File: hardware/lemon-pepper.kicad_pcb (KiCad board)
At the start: 4 copper layers, 35 x 35 mm, 76 parts, among them J101 INPUT, J201 USB_C_Receptacle_USB2.0, J301 TagConnect, M101 MOT, Q501 MMBT5551, U201 SRV05-4, U301 STM32G431, U302 SN65HVD230, U401 MT6835, U501 MAX15062CATA+T, U601 L6226QTR, U701 ACS711KEXLT-31AB-T, U702 ACS711KEXLT-31AB-T, U703 ACS711KEXLT-31AB-T, Y301 12MHz

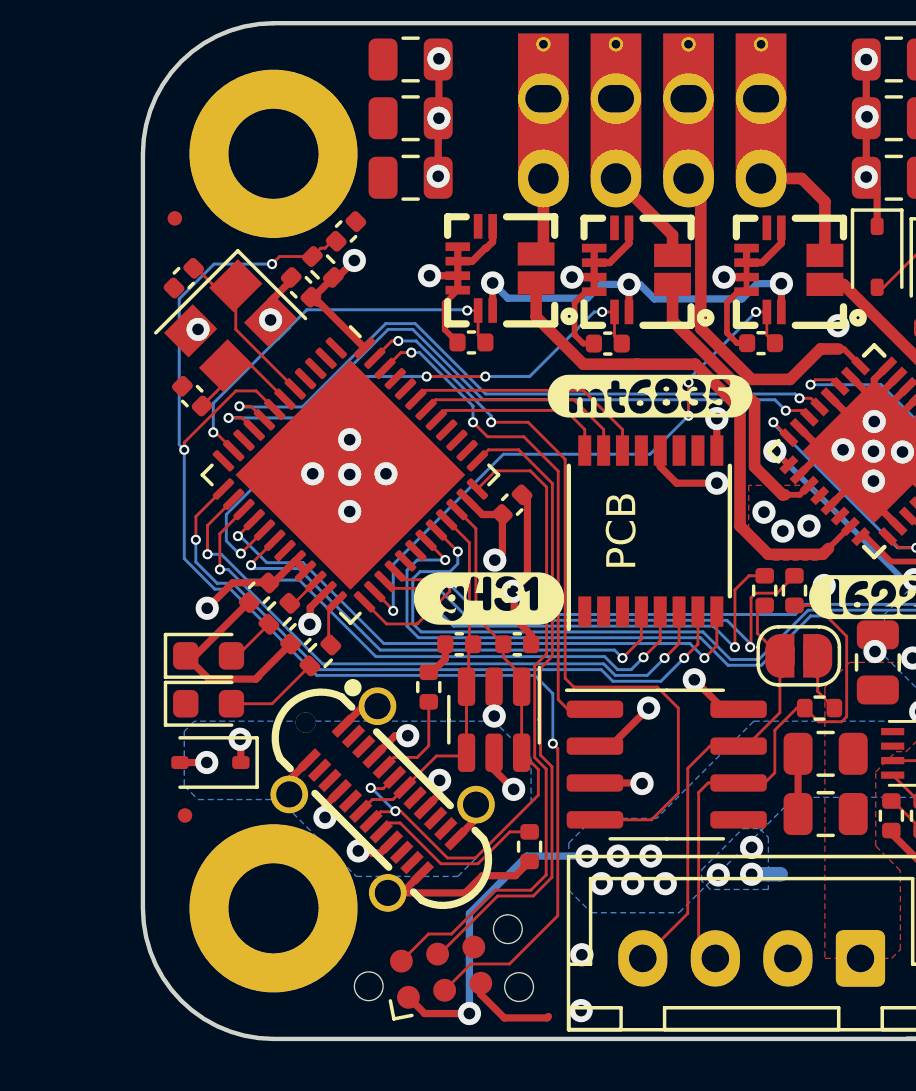
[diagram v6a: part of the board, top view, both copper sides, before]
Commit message: tweak pours
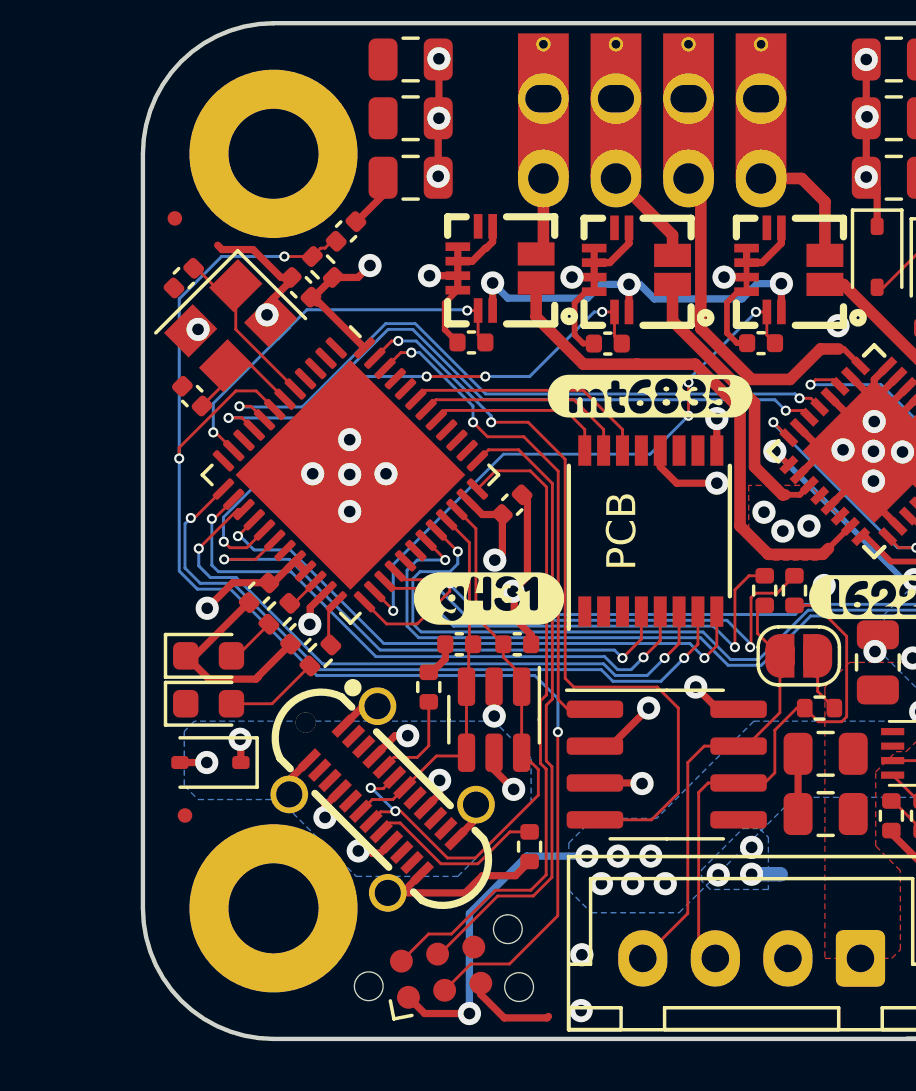
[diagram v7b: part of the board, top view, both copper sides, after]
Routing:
- net GND: track 91.0 -> 95.8 mm
- net +3V3: track 82.0 -> 86.2 mm
- net /encoder/CAL_EN: track 17.2 -> 19.0 mm
- net /encoder/COPI: track 21.3 -> 22.4 mm
- net /mcu/RESET: track 47.0 -> 47.7 mm
- net /encoder/SCK: track 23.6 -> 24.3 mm

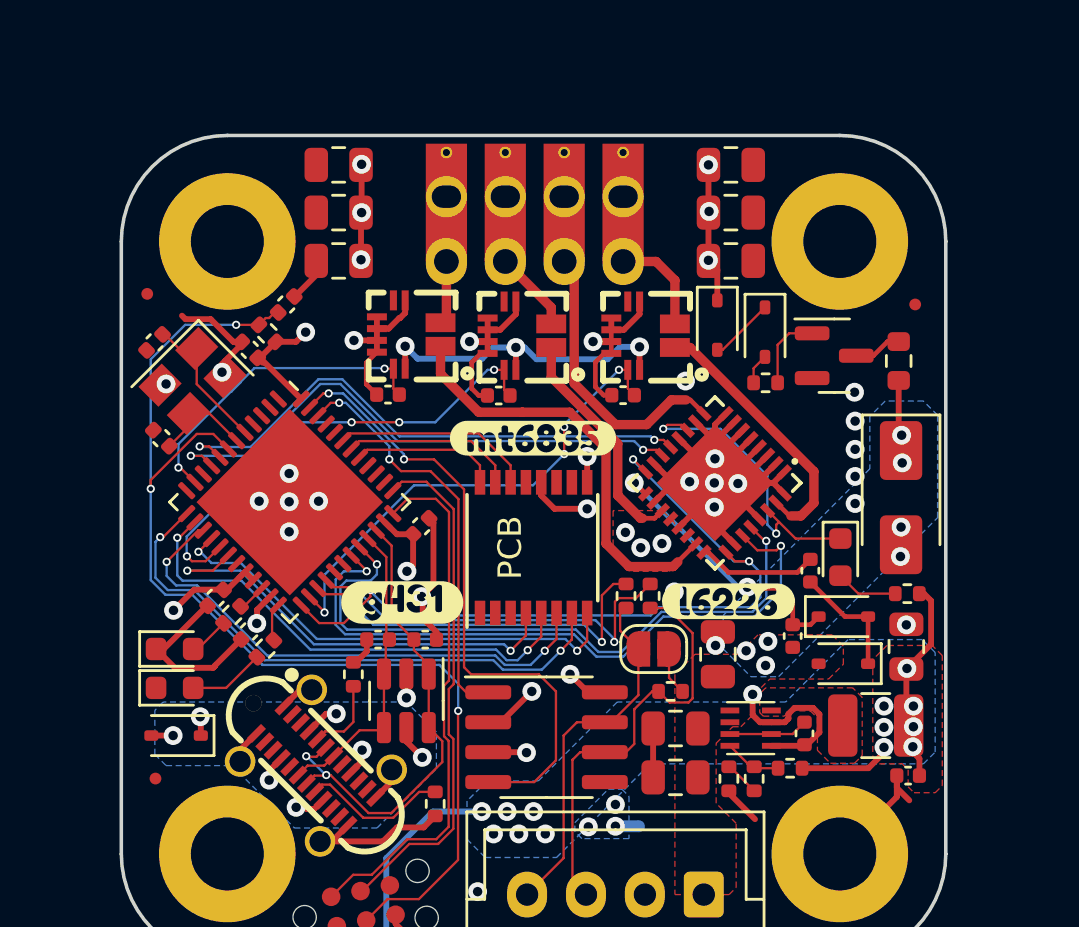
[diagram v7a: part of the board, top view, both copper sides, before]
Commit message: work on analog layout
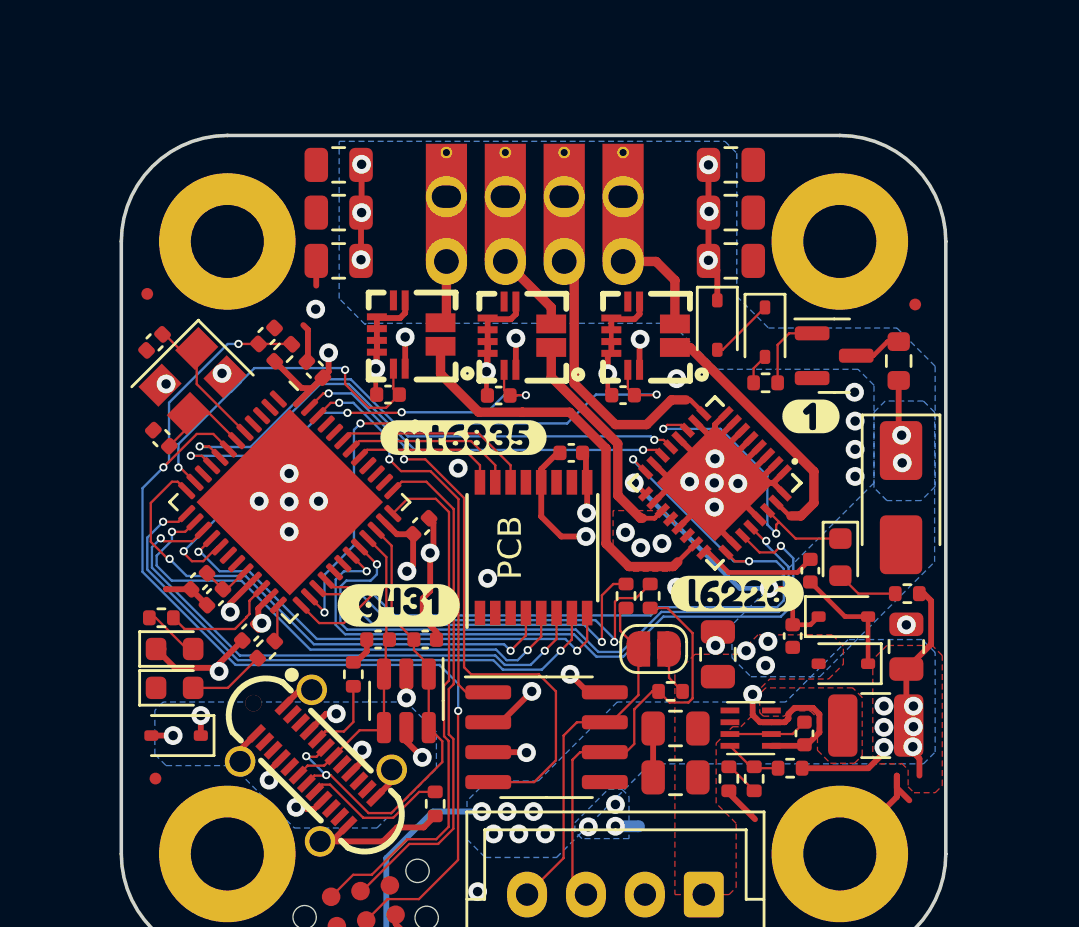
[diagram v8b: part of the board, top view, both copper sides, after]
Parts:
- added C307: 100n, Capacitor_SMD:C_0402_1005Metric, F.Cu at (132.8, 89.1)
- added kibuzzard-653468FC: G***, kibuzzard-653468FC, F.Cu at (158.1, 81.4)
- C301: value 100n -> 1u
- moved kibuzzard-65306358 21.7 mm to (146.1, 77.0)
- moved C401 19.8 mm to (147.9, 83.0)
- moved C303 10.6 mm to (137.0, 79.4), turned to 135 degrees
- moved C301 10.1 mm to (132.1, 88.4), turned to -135 degrees
- moved R301 3.00 mm to (130.5, 90.0), turned to 180 degrees
- moved kibuzzard-652C580D 2.95 mm to (143.3, 82.3)
- moved G*** 2.22 mm to (146.6, 87.8)
- moved C308 1.58 mm to (135.0, 78.0)
- moved R306 1.07 mm to (135.7, 78.7), turned to 45 degrees
- moved kibuzzard-65305A5A 0.50 mm to (154.9, 88.9)
- moved kibuzzard-652C57F7 0.20 mm to (140.6, 89.4)
- moved C302 0.07 mm to (134.3, 90.6)
- moved R302 0.05 mm to (134.9, 91.3)
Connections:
- C301 pad 1: +3V3 -> Net-(U301-VREF+)
- U301 pad 12: unconnected-(U301-PA4-Pad12) -> /encoder/CAL_EN
- U301 pad 18: /encoder/CAL_EN -> unconnected-(U301-PB1-Pad18)
- U301 pad 20: +3V3 -> Net-(U301-VREF+)
- U401 pad 12: GNDA -> GND
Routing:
- net +3V3: track 86.2 -> 52.4 mm, vias 23 -> 22
- net Vmot: track 38.5 -> 43.7 mm
- net GNDA: track 24.1 -> 19.9 mm, vias 7 -> 6
- net /current sense/V_SENSE: track 20.9 -> 24.8 mm
- net Net-(U301-PB10): track 1.22 -> 5.00 mm
- net /encoder/CAL_EN: track 19.0 -> 22.8 mm
- net /mcu/RESET: track 47.7 -> 45.3 mm
- net Net-(U301-VREF+): track 0.00 -> 2.25 mm
- net /half bridges/ENA: track 31.7 -> 33.9 mm
- net /current sense/U_SENSE: track 13.6 -> 15.2 mm
- net /encoder/COPI: track 22.4 -> 23.9 mm
- net /half bridges/IN2A: track 27.6 -> 29.1 mm
- net /encoder/CIPO: track 21.0 -> 22.3 mm
- net /half bridges/IN1A: track 28.8 -> 30.0 mm
- net /current sense/W_SENSE: track 20.2 -> 21.2 mm
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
